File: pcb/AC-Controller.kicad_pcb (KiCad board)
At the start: 2 copper layers, 66 x 67 mm, 81 parts, among them J1 Serial, J2 USB_C_Top, J3 USB_C_Bottom, Q1 AO3400A, Q2 AO3401A, Q3 AO3400A, Q4 AO3400A, Q5 AO3400A, SW1 Mode, SW2 Value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

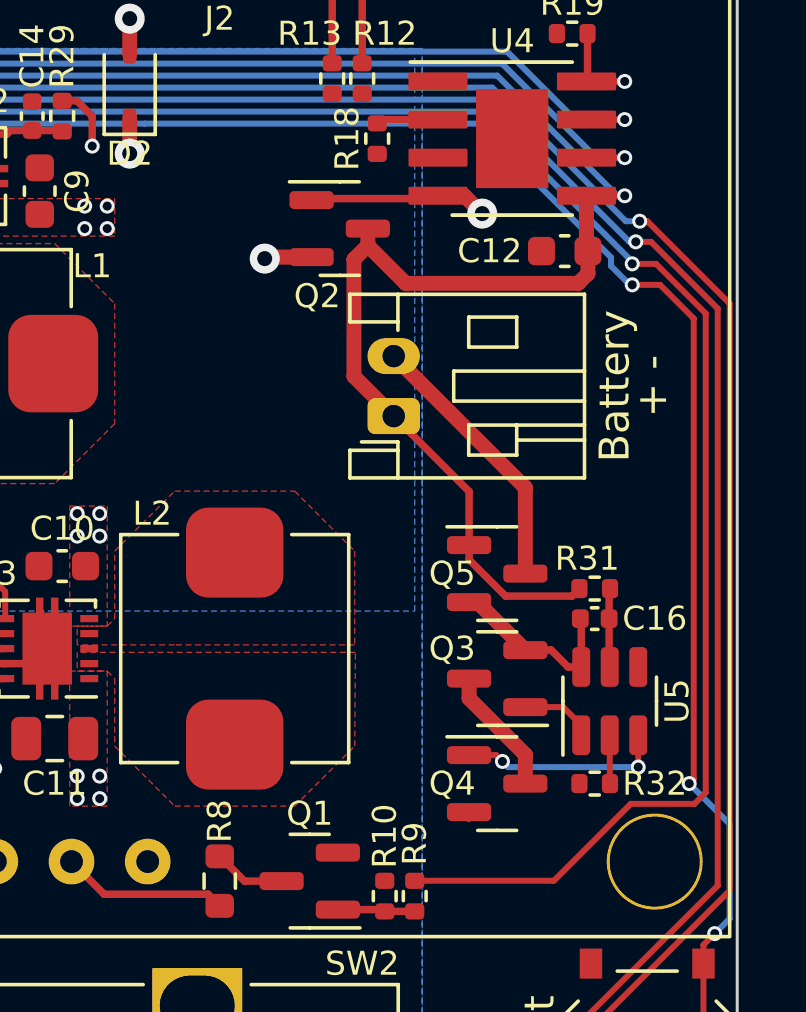
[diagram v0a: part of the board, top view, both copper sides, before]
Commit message: feat: remove battery protection IC
Since I only use protected battery packs (which is highly recommended) the additional protection IC on the PCB was obsolete and only raised production cost.
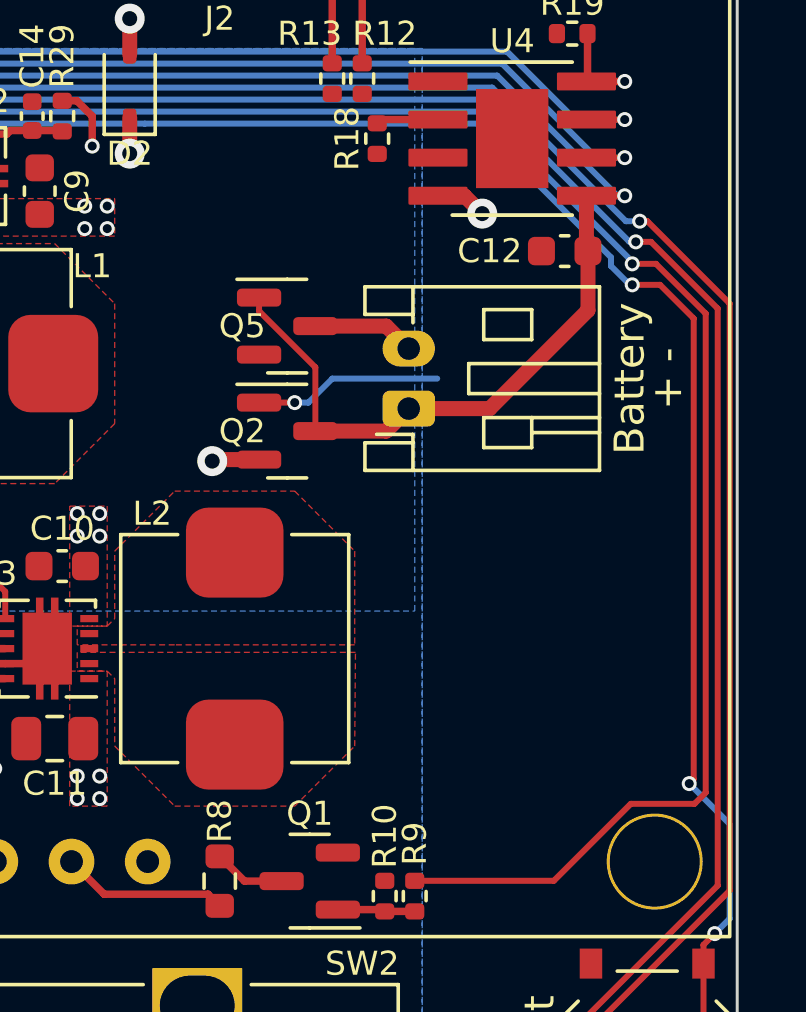
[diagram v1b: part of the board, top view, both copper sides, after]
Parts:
- removed C16: 100n, Capacitor_SMD:C_0402_1005Metric
- removed Q3, Q4: AO3400A, Package_TO_SOT_SMD:SOT-23
- removed R31: 100R, Resistor_SMD:R_0402_1005Metric
- removed R32: 1k, Resistor_SMD:R_0402_1005Metric
- removed U5: DW01A, Package_TO_SOT_SMD:SOT-23-6
- moved Q5 10.8 mm to (168.0, 88.0)
- moved Q2 6.97 mm to (168.0, 91.5)
- moved BT1 0.56 mm to (172.1, 90.8)
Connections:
- Q5 pad 2: /Power/B_{GND} -> GND
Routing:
- net /Battery+: track 95.6 -> 87.7 mm
- net /Power/OC: track 6.87 -> 0.00 mm, vias 2 -> 0
- net /Power/B_{GND}: track 6.26 -> 0.00 mm
- net /Power/B-: track 9.07 -> 3.42 mm
- net Net-(Q3-D): track 4.28 -> 0.00 mm
- net Net-(U5-VCC): track 2.63 -> 0.00 mm
- net /Power/OD: track 2.45 -> 0.00 mm
- net /Power/V_{BUS}: track 19.9 -> 21.9 mm, vias 7 -> 8
- net /Power/VM: track 1.62 -> 0.00 mm
- net GND: track 6.97 -> 6.35 mm

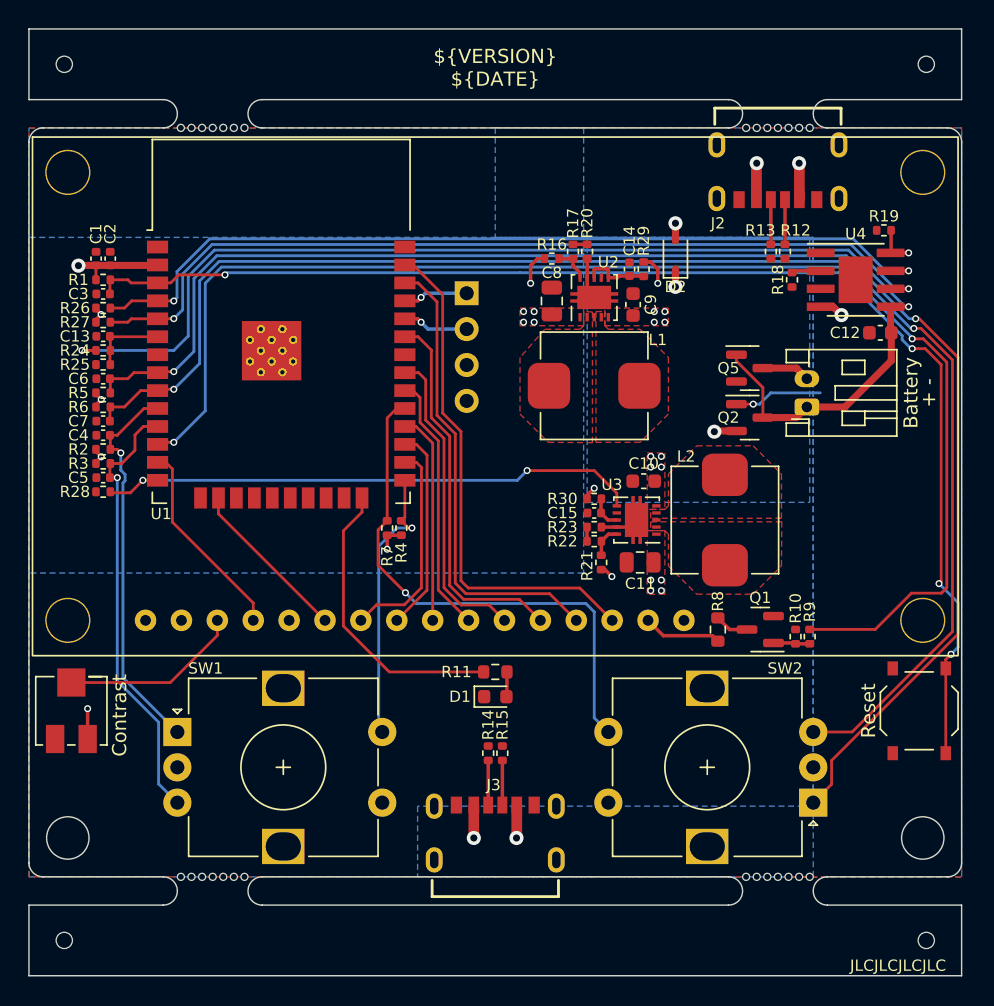
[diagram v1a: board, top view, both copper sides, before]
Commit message: feat: add charging indicator LED
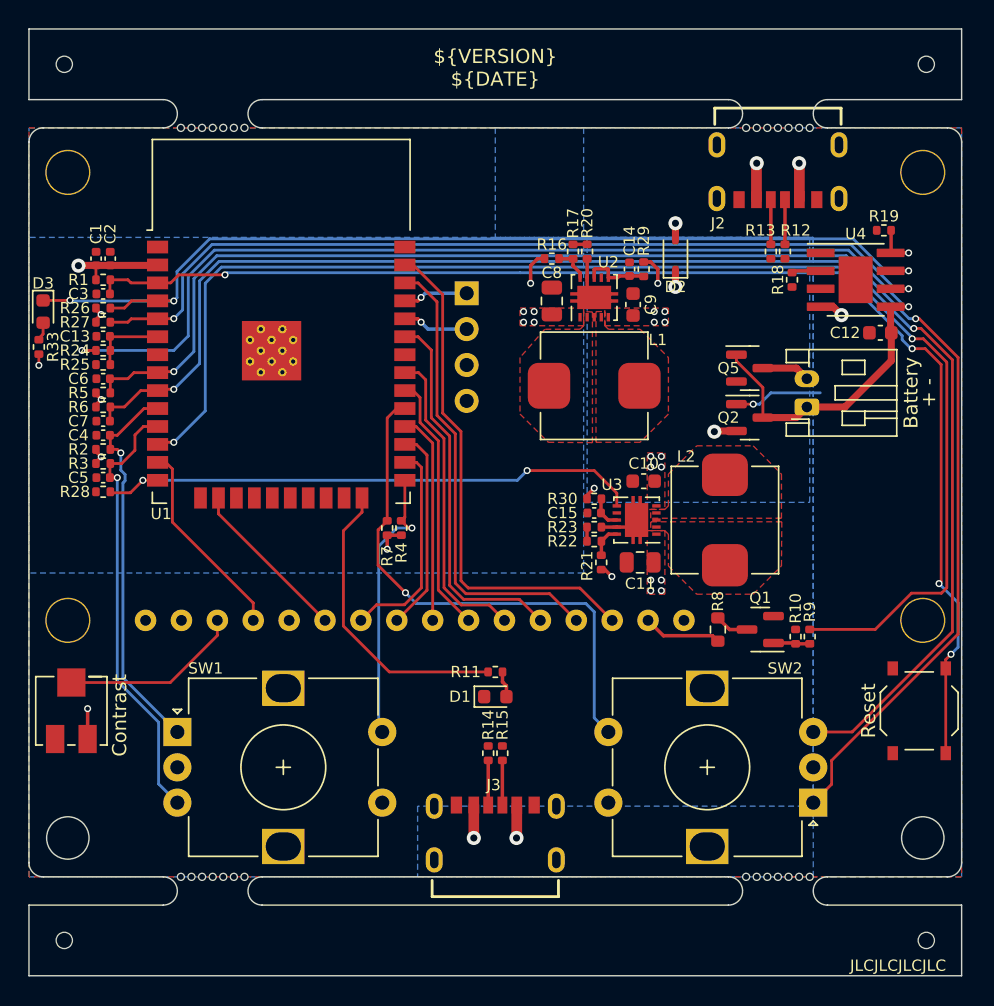
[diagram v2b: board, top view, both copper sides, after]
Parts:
- added D3: Charging, LED_SMD:LED_0603_1608Metric, F.Cu at (118.0, 84.0)
- added R33: 680R, Resistor_SMD:R_0402_1005Metric, F.Cu at (117.7, 86.5)
- R11: footprint Resistor_SMD:R_0603_1608Metric -> Resistor_SMD:R_0402_1005Metric
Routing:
- net /~{Battery_Charging}: track 61.8 -> 71.1 mm, vias 2 -> 3
- net Net-(D3-A): track 0.00 -> 1.38 mm
- net +3V3: track 15.0 -> 15.8 mm, vias 10 -> 11

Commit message: feat: replace contrast pot with more common type
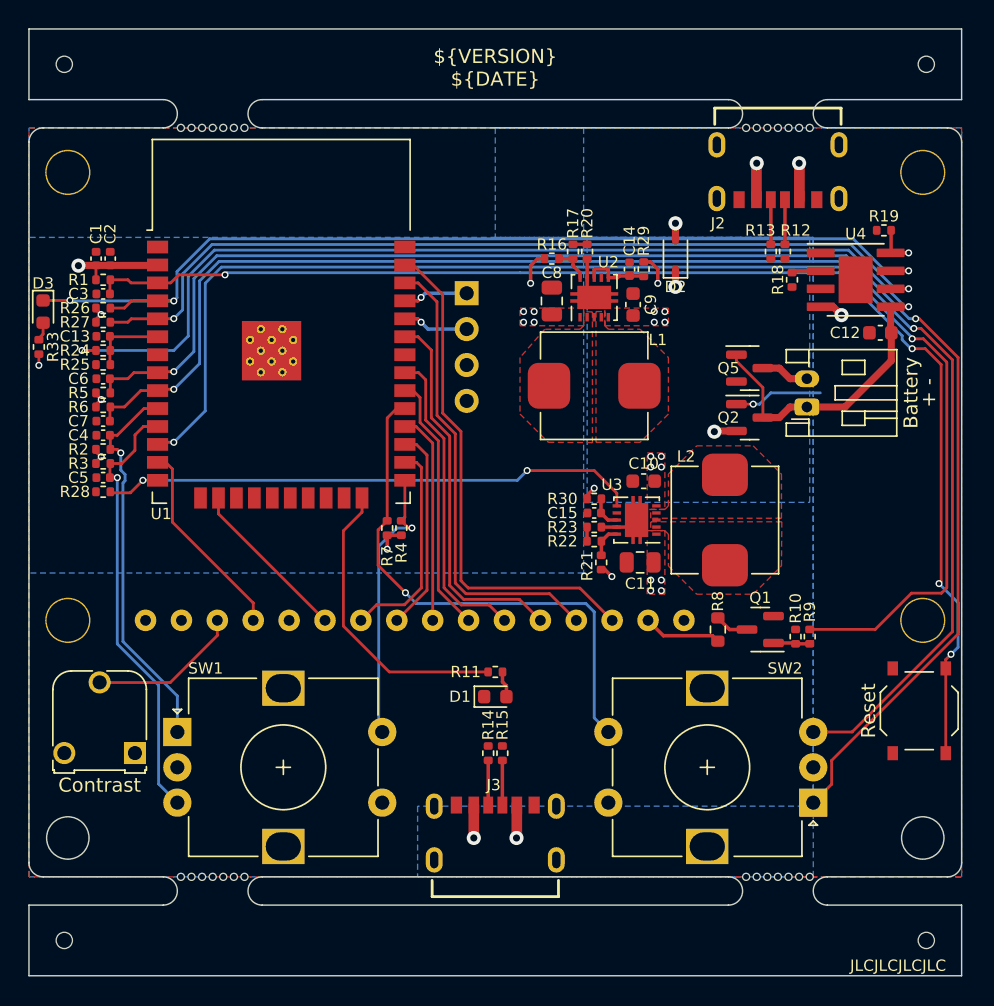
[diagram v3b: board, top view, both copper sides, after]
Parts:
- RV1: footprint Potentiometer_SMD:Potentiometer_Bourns_3224J_Horizontal -> Potentiometer_THT:Potentiometer_Runtron_RM-065_Vertical
- moved RV1 5.40 mm to (124.5, 115.2), turned to 180 degrees
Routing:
- net +5V: track 3.10 -> 0.95 mm, vias 6 -> 5
- net /LCD_VO: track 12.8 -> 10.8 mm

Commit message: feat: replace TP4056 Prog Resistor footprint with 0603
Replace the footprint for the programming resistor to 0603 to make replacing it easier. Also changing the default value to 4.7k for slower charge and less heat production
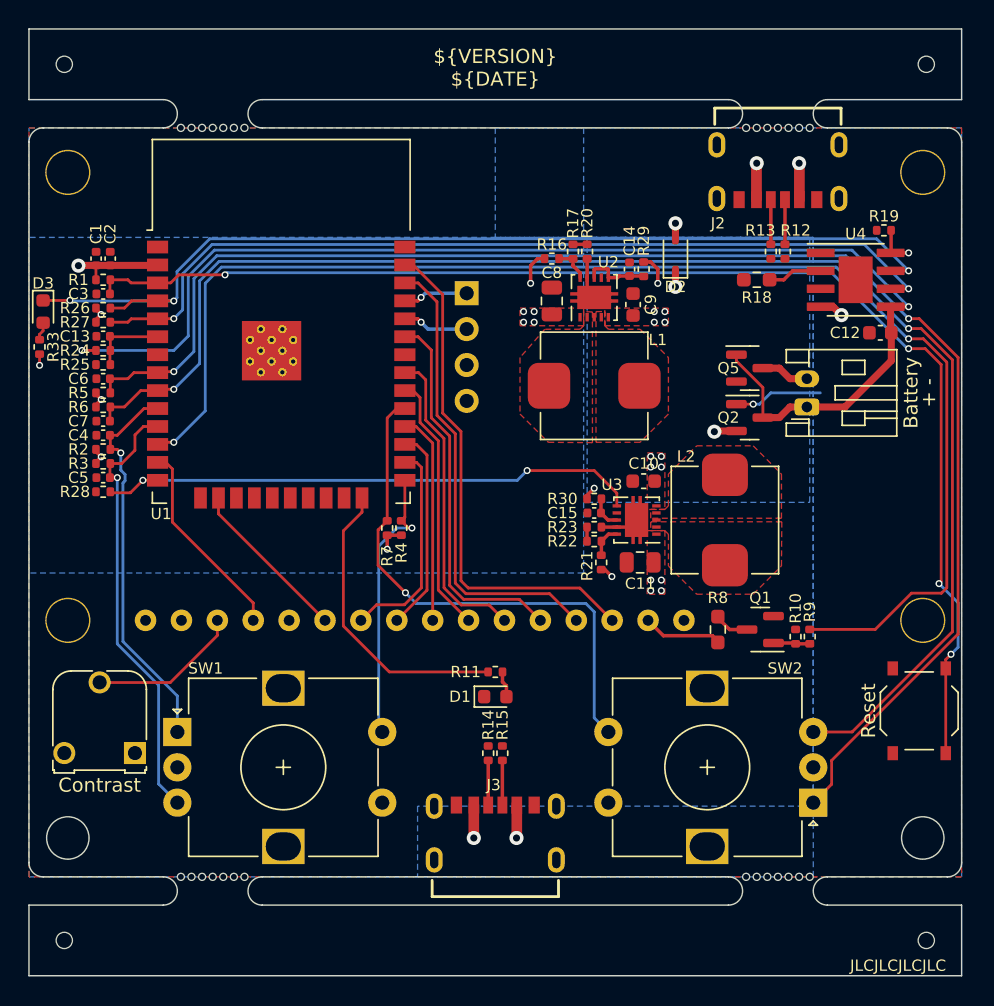
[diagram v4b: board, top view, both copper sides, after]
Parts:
- R18: value 2k -> 4k7; footprint Resistor_SMD:R_0402_1005Metric -> Resistor_SMD:R_0603_1608Metric_Pad0.98x0.95mm_HandSolder
- R8: footprint Resistor_SMD:R_0603_1608Metric -> Resistor_SMD:R_0603_1608Metric_Pad0.98x0.95mm_HandSolder
- moved R18 2.50 mm to (168.5, 81.8), turned to 180 degrees
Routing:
- net /Power/PROG: track 2.08 -> 3.88 mm

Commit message: feat: add cutout for battery cable
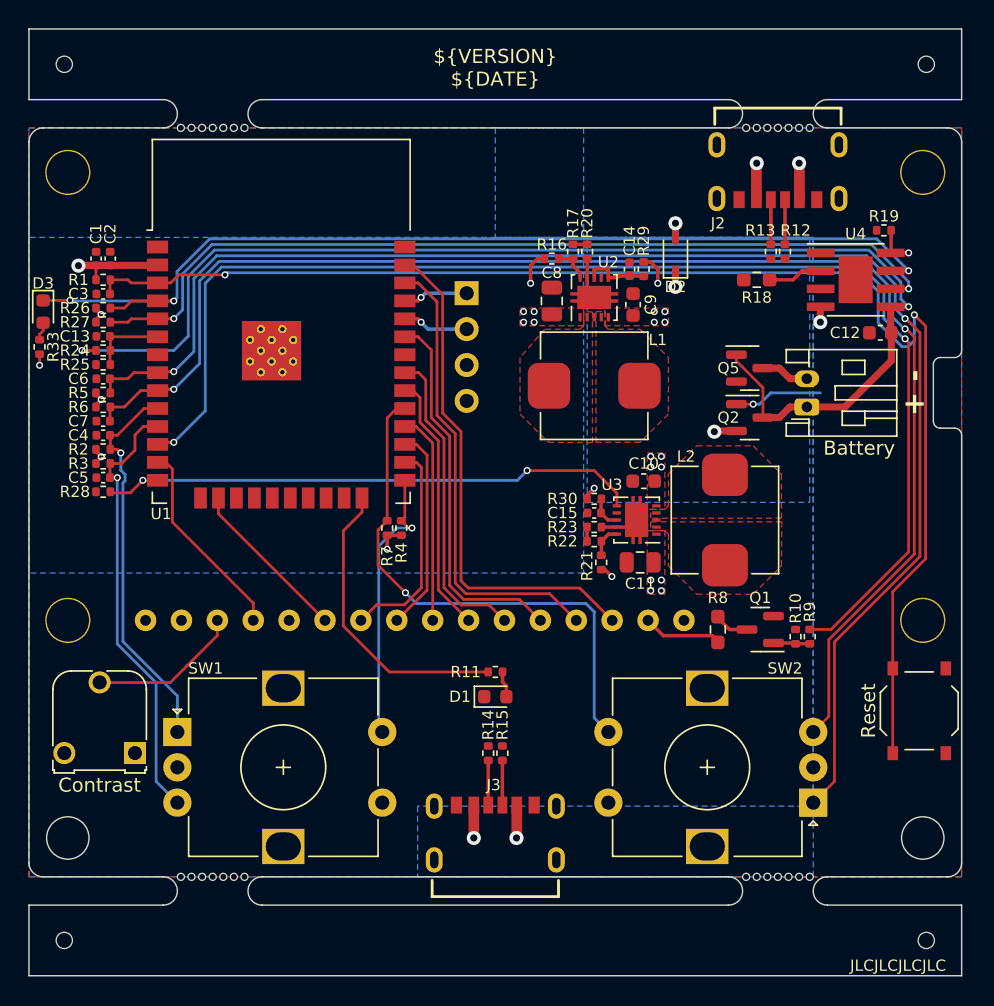
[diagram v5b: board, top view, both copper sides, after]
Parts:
- turned SW3 to -90 degrees
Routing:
- net /LCD_BL: track 96.0 -> 91.2 mm
- net /EN: track 91.3 -> 96.0 mm, vias 4 -> 2
- net /Encoder2_B: track 103.2 -> 99.9 mm
- net /Encoder2_A: track 106.4 -> 104.6 mm
- net /Battery+: track 87.7 -> 88.4 mm
- net /Power/V_{BUS}: track 21.9 -> 21.3 mm
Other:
- outline, holes or cut-outs redrawn

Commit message: feat: add disable jumper for battery charger
Adding a jumper to disable the TP4056 Battery Charger IC in case no battery is connected and the device is powered by USB only. No need for the IC to draw power in that case.
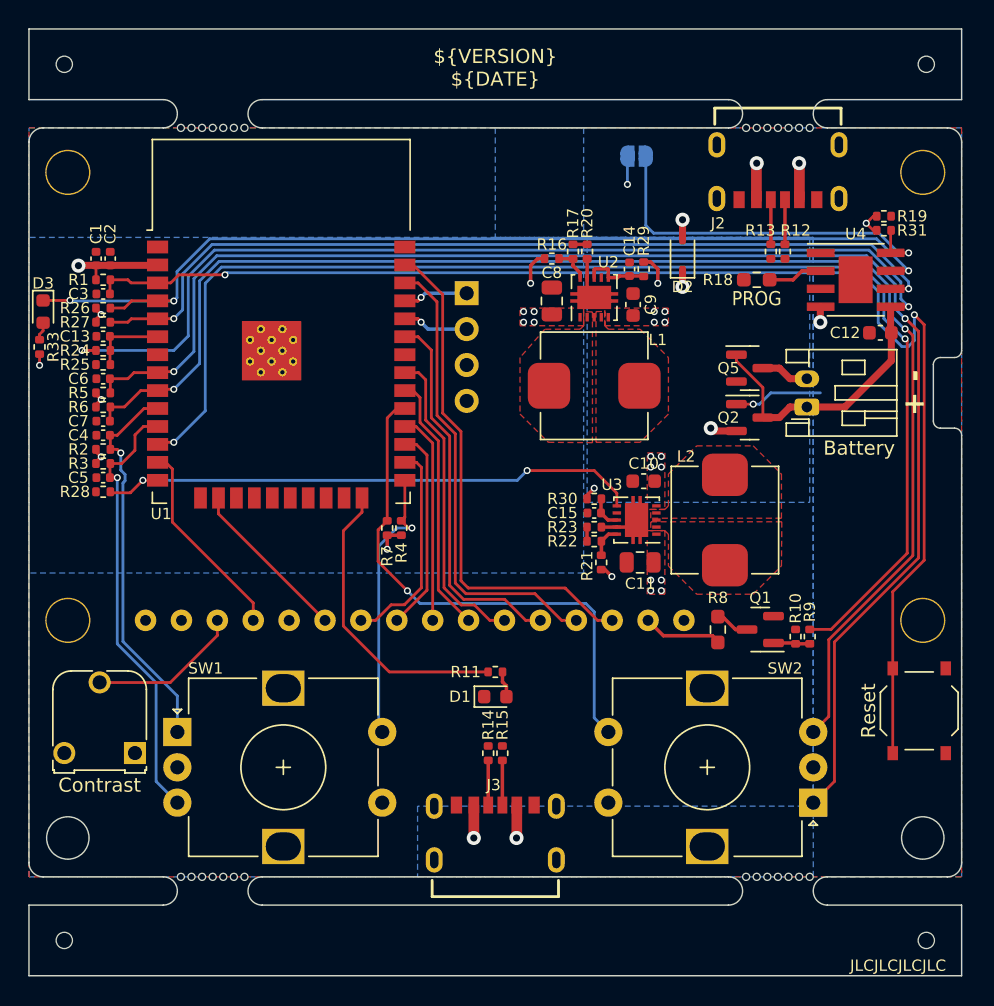
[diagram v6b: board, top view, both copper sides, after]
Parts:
- added JP1: TP4056_Disable, Jumper:SolderJumper-2_P1.3mm_Open_RoundedPad1.0x1.5mm, B.Cu at (160.0, 73.0)
- added R31: 100k, Resistor_SMD:R_0402_1005Metric, F.Cu at (177.5, 78.2)
- BT1: value LiIon -> LiPo
- moved R19 1.00 mm to (177.5, 77.2), turned to 0 degrees
- moved D2 0.50 mm to (163.2, 80.0)
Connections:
- net /EN renamed /~{RESET}
- U4 pad 8: /Power/V_{BUS} -> /Power/TP_CE
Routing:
- net /Power/TP_CE: track 0.00 -> 27.2 mm, vias 0 -> 1
- net GND: track 6.35 -> 8.35 mm, vias 0 -> 1
- net /Power/V_{BUS}: track 21.3 -> 20.6 mm
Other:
- board text added: "Disable Battery Charging Circuit"
- board text added: "IoT Remote"
- board text added: "PROG"
- board text removed: "Qeteshs IoT Remote"

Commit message: style: board and schematics cleanup
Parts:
- moved SW3 1.68 mm to (178.5, 113.0), turned to 180 degrees
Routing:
- net /~{RESET}: track 96.0 -> 100.2 mm
- net /LCD_EN: track 11.8 -> 12.4 mm
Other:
- board text added: "IO0"
